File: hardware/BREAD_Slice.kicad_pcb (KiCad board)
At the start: 2 copper layers, 72.6 x 100 mm, 16 parts, among them J1 Conn_01x10_Female, J2 I2C_01x04

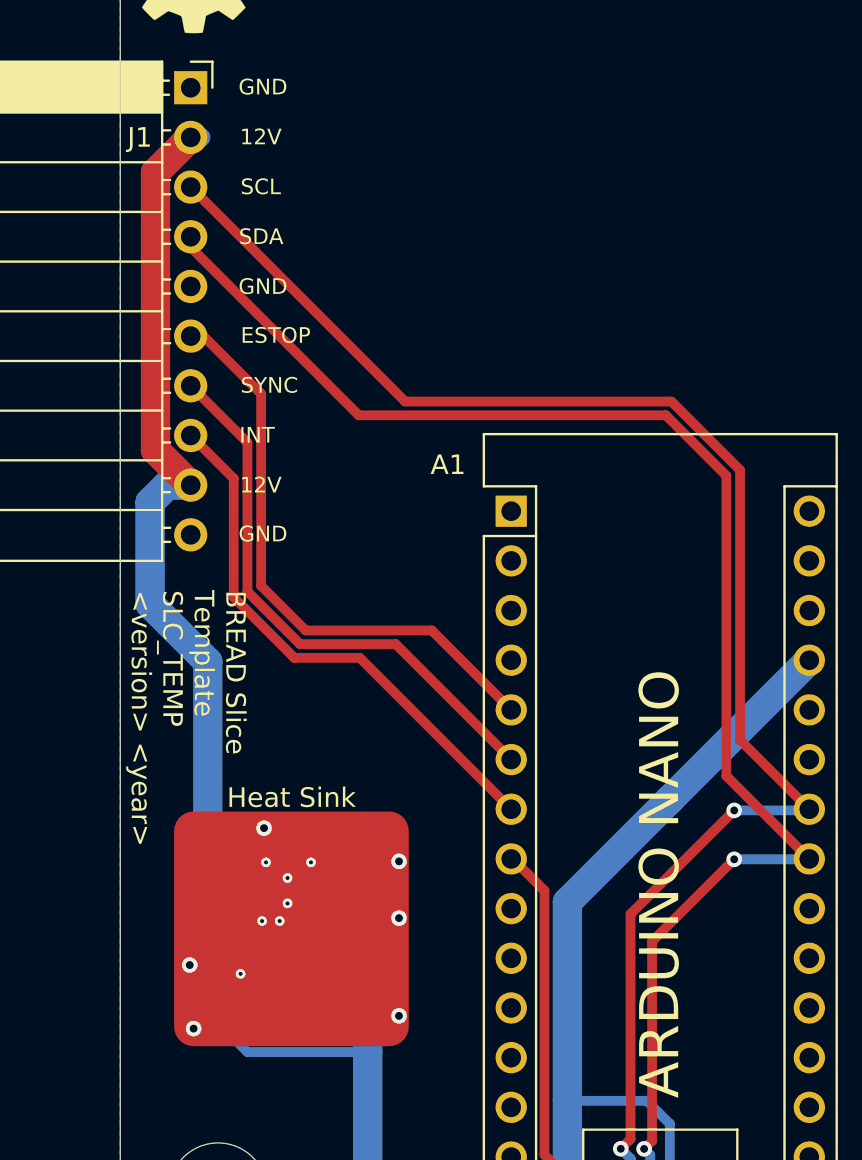
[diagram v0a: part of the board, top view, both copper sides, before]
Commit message: fixed 5-12V converter reinitializing placement when pcb is updated
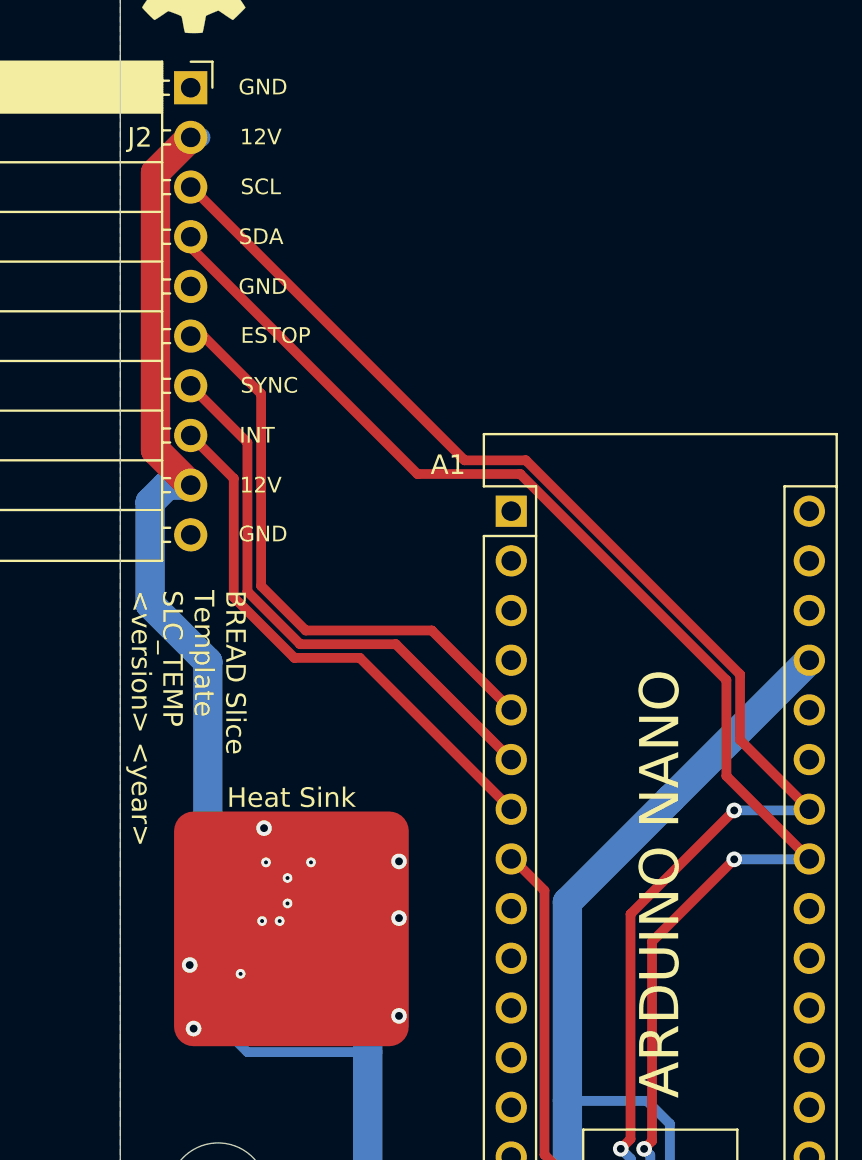
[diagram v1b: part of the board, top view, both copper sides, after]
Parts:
- HS1: footprint SparkFun-Fuse:Thermal Pad -> KML-Custom:Thermal Pad
- renumbered J2 to J1, J1 to J2
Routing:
- net /I2C_CLK: track 78.5 -> 72.3 mm
- net /I2C_DAT: track 76.6 -> 70.5 mm

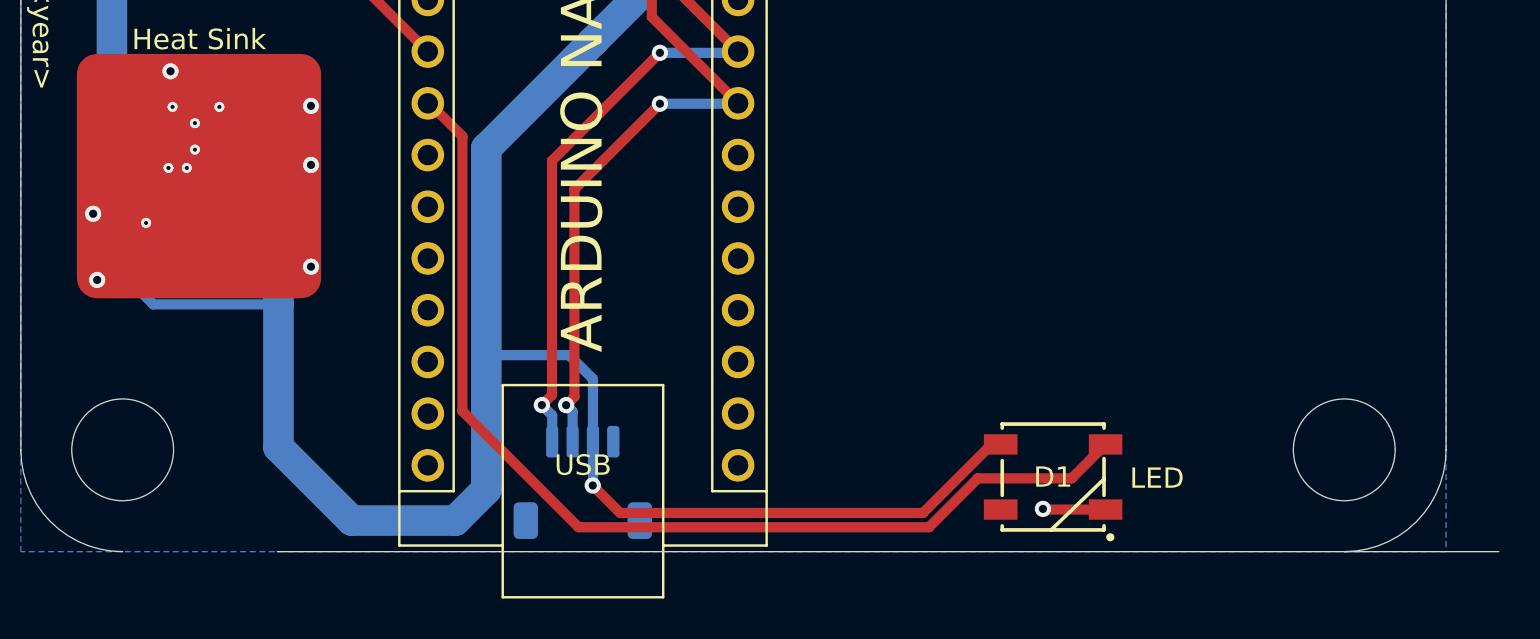
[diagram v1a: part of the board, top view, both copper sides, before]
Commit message: clear all DRC errors related to via placement and rules and also misplaced edge cuts
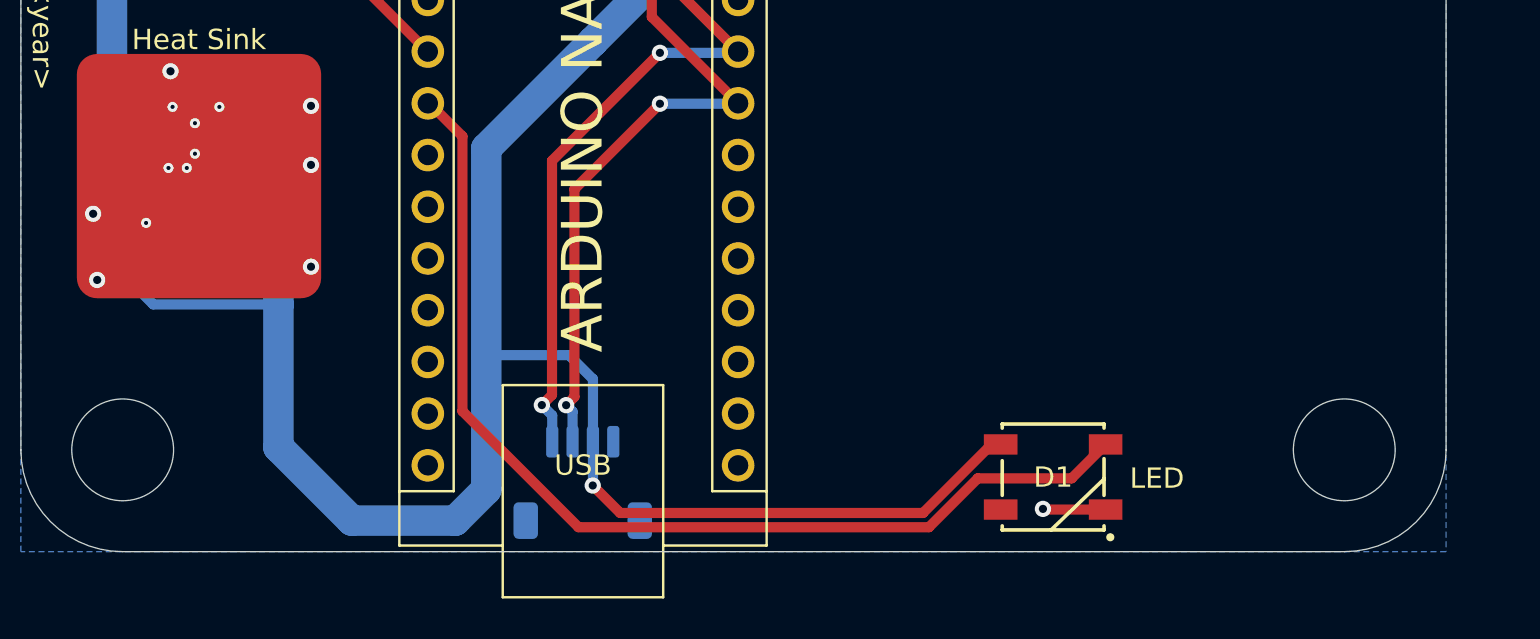
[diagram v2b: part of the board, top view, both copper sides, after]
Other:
- board size 72.6 x 100 mm -> 70 x 100 mm
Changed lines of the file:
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@@
 		(tags "TSOT TO_SOT_SMD")
 		(property "Reference" "U1"
-			(at 0 2.4 360)
+			(at 0 2.4 0)
 			(layer "B.SilkS")
 			(effects
@@
 		)
 		(fp_text user "${REFERENCE}"
-			(at 0 0 360)
+			(at 0 0 0)
 			(layer "B.Fab")
 			(effects
@@
 		(tags "capacitor")
 		(property "Reference" "C3"
-			(at 0 1.85 360)
+			(at 0 1.85 0)
 			(layer "B.SilkS")
 			(effects
@@
 		)
 		(property "Value" "22uF"
-			(at 0 -1.85 360)
+			(at 0 -1.85 0)
 			(layer "B.Fab")
 			(effects
@@
 		)
 		(fp_text user "${REFERENCE}"
-			(at 0 0 360)
+			(at 0 0 0)
 			(layer "B.Fab")
 			(effects
@@
 		(tags "capacitor")
 		(property "Reference" "C4"
-			(at 0 1.85 360)
+			(at 0 1.85 0)
 			(layer "B.SilkS")
 			(effects
@@
 		)
 		(property "Value" "22uF"
-			(at 0 -1.85 360)
+			(at 0 -1.85 0)
 			(layer "B.Fab")
 			(effects
@@
 		)
 		(fp_text user "${REFERENCE}"
-			(at 0 0 360)
+			(at 0 0 0)
 			(layer "B.Fab")
 			(effects
@@
 		)
 		(property "Value" "4.7uH"
-			(at 0 -2.28 360)
+			(at 0 -2.28 0)
 			(layer "B.Fab")
 			(effects
@@
 		)
 		(fp_text user "${REFERENCE}"
-			(at 0 0 360)
+			(at 0 0 0)
 			(layer "B.Fab")
 			(effects
@@
 	(gr_line
 		(start 160.188 139.8)
-		(end 195.188 139.8)
+		(end 187.6 139.8)
 		(stroke
 			(width 0.05)
@@
 	)
 	(gr_line
-		(start 135.188 139.8)
+		(start 127.6 139.8)
 		(end 160.188 139.8)
 		(stroke
@@
 		)
 	)
-	(dimension
-		(type aligned)
-		(layer "B.Cu")
-		(pts
-			(xy 127.6 44.8) (xy 187.6 44.8)
-		)
-		(height -5.6)
-		(gr_text "60.0000 mm"
-			(at 157.6 37.4 0)
-			(layer "B.Cu")
-			(effects
-				(font
-					(size 1.5 1.5)
-					(thickness 0.3)
-				)
-			)
-		)
-		(format
-			(prefix "")
-			(suffix "")
-			(units 3)
-			(units_format 1)
-			(precision 4)
-		)
-		(style
-			(thickness 0.2)
-			(arrow_length 1.27)
-			(text_position_mode 0)
-			(extension_height 0.58642)
-			(extension_offset 0.5) keep_text_aligned)
-	)
-	(dimension
-		(type aligned)
-		(layer "B.Cu")
-		(pts
-			(xy 179.6 21.6) (xy 249 21.6)
-		)
-		(height 3.2)
-		(gr_text "69.4000 mm"
-			(at 214.3 23 0)
-			(layer "B.Cu")
-			(effects
-				(font
-					(size 1.5 1.5)
-					(thickness 0.3)
-				)
-			)
-		)
-		(format
-			(prefix "")
-			(suffix "")
-			(units 3)
-			(units_format 1)
-			(precision 4)
-		)
-		(style
-			(thickness 0.2)
-			(arrow_length 1.27)
-			(text_position_mode 0)
-			(extension_height 0.58642)
-			(extension_offset 0.5) keep_text_aligned)
-	)
 	(segment
 		(start 172.8 137.7)
@@
 	)
 	(via
-		(at 131.15 120.055)
+		(at 131.15 120.255)
 		(size 0.5)
 		(drill 0.2)
@@
 	)
 	(segment
-		(start 131.15 119.455)
-		(end 131.15 118.755)
-		(width 0.5)
-		(layer "B.Cu")
-		(net 3)
-	)
-	(segment
 		(start 131 121.805)
 		(end 131.15 121.655)
@@
 	)
 	(segment
-		(start 131.15 119.455)
-		(end 131.15 120.055)
-		(width 0.5)
-		(layer "B.Cu")
-		(net 3)
-	)
-	(segment
 		(start 129.85 120.955)
 		(end 128.95 120.955)
@@
 	(segment
 		(start 131.15 119.455)
-		(end 132.375 119.455)
-		(width 1)
-		(layer "B.Cu")
-		(net 3)
-	)
-	(segment
-		(start 130.025 119.455)
-		(end 131.15 119.455)
-		(width 1)
-		(layer "B.Cu")
-		(net 3)
-	)
-	(segment
-		(start 131.15 120.055)
 		(end 131.15 120.255)
 		(width 0.5)
 		(layer "B.Cu")
 		(net 3)
+	)
+	(segment
+		(start 131.15 119.455)
+		(end 131.15 118.755)
+		(width 0.5)
+		(layer "B.Cu")
+		(net 3)
+	)
+	(segment
+		(start 130.025 119.455)
+		(end 132.375 119.455)
+		(width 1.5)
+		(layer "B.Cu")
+		(net 3)

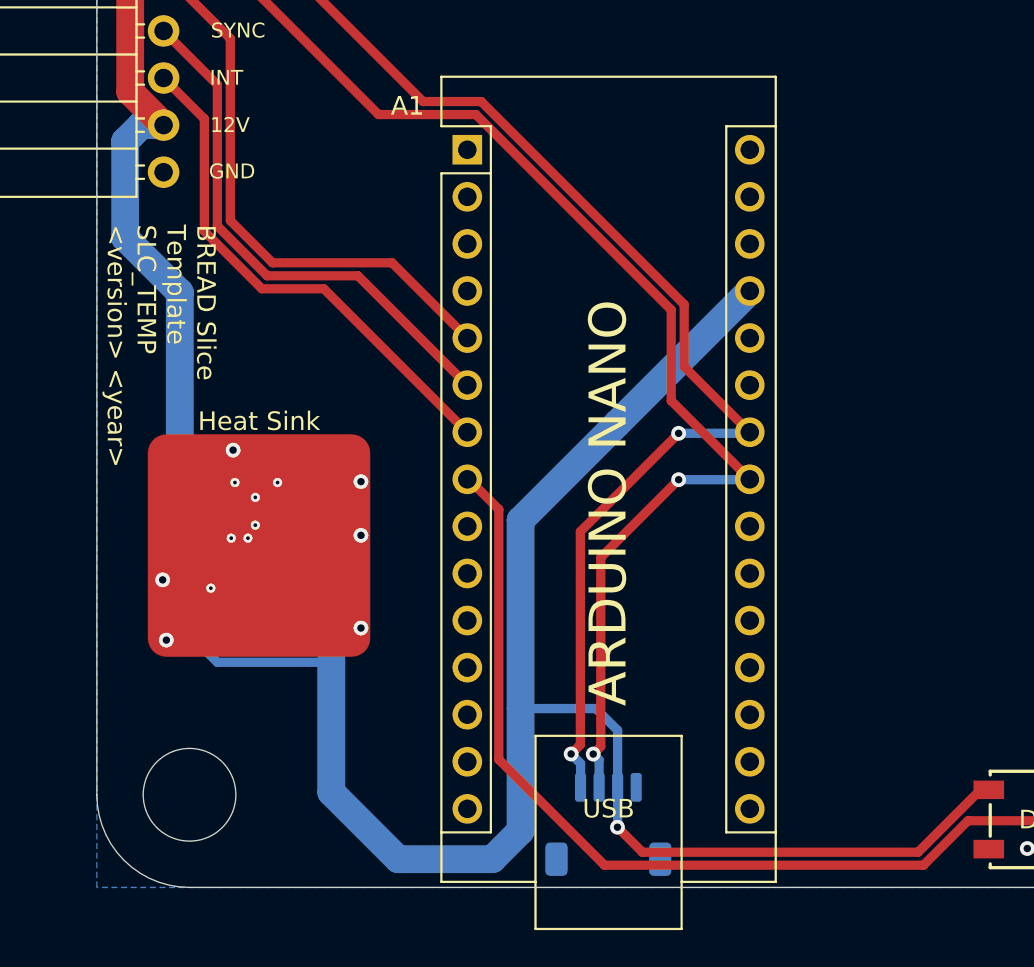
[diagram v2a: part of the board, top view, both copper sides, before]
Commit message: changed i2c connection to jst to simplify
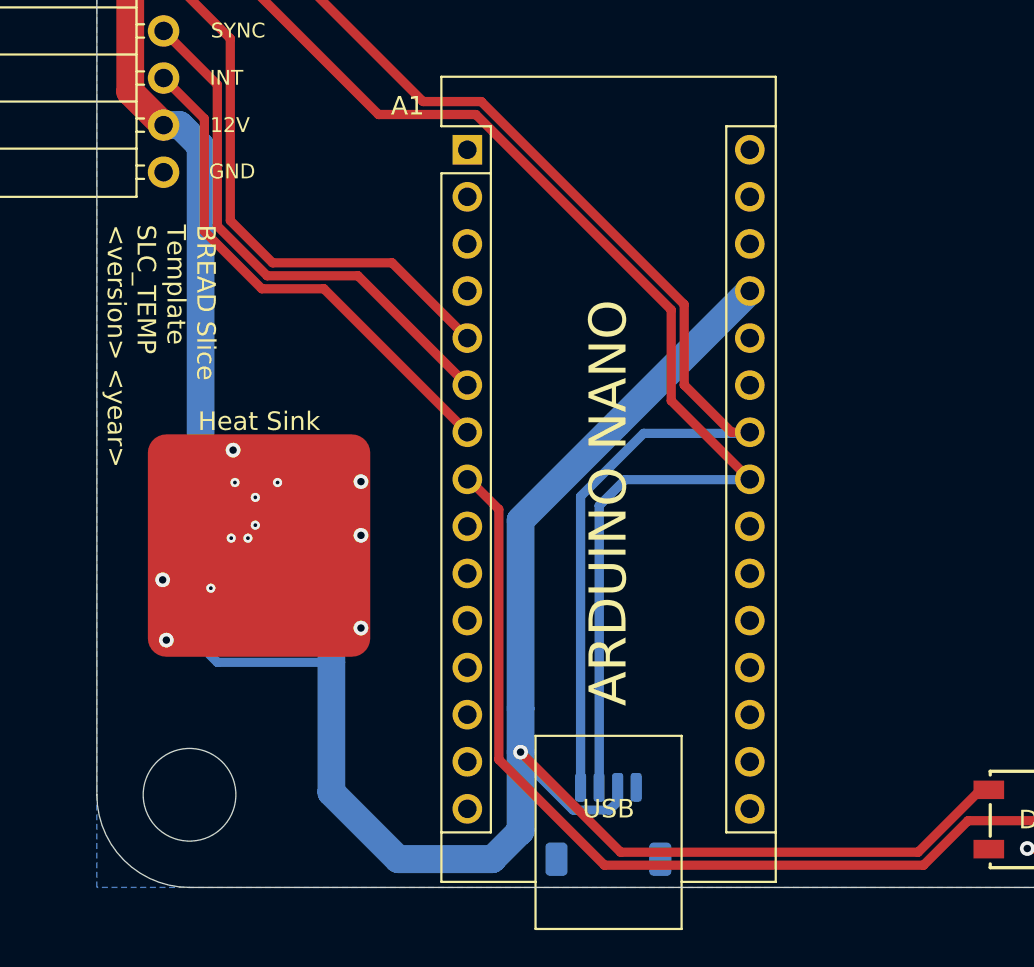
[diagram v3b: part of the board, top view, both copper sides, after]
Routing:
- net +5V: track 108.9 -> 112.5 mm
- net /I2C_DAT: track 70.5 -> 71.9 mm, vias 2 -> 0
- net /I2C_CLK: track 72.3 -> 73.6 mm, vias 2 -> 0
- net +12V: track 46.8 -> 45.9 mm
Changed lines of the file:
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@@
-	)
-	(segment
-		(start 152.0375 137.9)
-		(end 150.688 136.5505)
-		(width 0.5)
-		(layer "F.Cu")
-		(net 5)
 	)
 	(segment
@@
 	(segment
 		(start 166.91005 137.9)
-		(end 152.0375 137.9)
+		(end 150.86 137.9)
 		(width 0.5)
 		(layer "F.Cu")
@@
 	)
 	(segment
+		(start 150.86 137.9)
+		(end 145.46 132.5)
+		(width 0.5)
+		(layer "F.Cu")
+		(net 5)
+	)
+	(segment
 		(start 157.808 107.62)
 		(end 157.828 107.62)
@@
 	)
 	(via
-		(at 150.688 136.5505)
+		(at 145.46 132.5)
 		(size 0.8)
 		(drill 0.4)
@@
 	)
 	(segment
+		(start 145.46 132.789684)
+		(end 148.295316 135.625)
+		(width 0.5)
+		(layer "B.Cu")
+		(net 5)
+	)
+	(segment
 		(start 157.828 107.62)
 		(end 150.698 114.75)
@@
 	)
 	(segment
+		(start 150.247999 135.625)
+		(end 150.698 135.174999)
+		(width 0.5)
+		(layer "B.Cu")
+		(net 5)
+	)
+	(segment
 		(start 143.936 138.276)
 		(end 145.46 136.752)
@@
 	)
 	(segment
+		(start 145.46 132.5)
+		(end 145.46 132.789684)
+		(width 0.5)
+		(layer "B.Cu")
+		(net 5)
+	)
+	(segment
 		(start 135.25 127.655)
 		(end 129.103122 127.655)
@@
 	)
 	(segment
-		(start 149.524 130.148)
-		(end 145.46 130.148)
-		(width 0.5)
-		(layer "B.Cu")
-		(net 5)
-	)
-	(segment
 		(start 127.6125 126.164378)
 		(end 127.6125 123.705)
@@
 	)
 	(segment
-		(start 145.46 136.752)
+		(start 145.46 132.5)
 		(end 145.46 130.148)
 		(width 1.5)
-		(layer "B.Cu")
-		(net 5)
-	)
-	(segment
-		(start 150.698 134.4)
-		(end 150.698 131.322)
-		(width 0.5)
 		(layer "B.Cu")
 		(net 5)
@@
 	)
 	(segment
-		(start 150.698 136.5405)
-		(end 150.698 134.4)
-		(width 0.5)
-		(layer "B.Cu")
-		(net 5)
-	)
-	(segment
 		(start 135.3 116.48)
 		(end 135.3 119.43)
@@
 	)
 	(segment
+		(start 150.698 135.174999)
+		(end 150.698 134.4)
+		(width 0.5)
+		(layer "B.Cu")
+		(net 5)
+	)
+	(segment
 		(start 145.46 119.988)
 		(end 150.698 114.75)
@@
 	)
 	(segment
-		(start 150.688 136.5505)
-		(end 150.698 136.5405)
+		(start 148.295316 135.625)
+		(end 150.247999 135.625)
 		(width 0.5)
 		(layer "B.Cu")
@@
 	)
 	(segment
+		(start 145.46 136.752)
+		(end 145.46 132.5)
+		(width 1.5)
+		(layer "B.Cu")
+		(net 5)
+	)
+	(segment
 		(start 158.008 107.8)
 		(end 157.828 107.62)
@@
 	)
 	(segment
-		(start 150.698 131.322)
-		(end 149.524 130.148)
-		(width 0.5)
-		(layer "B.Cu")
-		(net 5)
-	)
-	(segment
 		(start 135.25 134.67)
 		(end 138.856 138.276)
@@
 	)
 	(segment
+		(start 156.84 115.24)
+		(end 154.288 112.688)
+		(width 0.5)
+		(layer "F.Cu")
+		(net 7)
+	)
+	(segment
 		(start 154.288 108.34805)
 		(end 143.33995 97.4)
@@
 	)
 	(segment
-		(start 154.288 111.7)
+		(start 157.828 115.24)
+		(end 156.84 115.24)
+		(width 0.5)
+		(layer "F.Cu")
+		(net 7)
+	)
+	(segment
+		(start 154.288 112.688)
 		(end 154.288 108.34805)
+		(width 0.5)
+		(layer "F.Cu")
+		(net 7)
+	)
+	(segment
+		(start 140.2 97.4)
+		(end 126.23 83.43)
 		(width 0.5)
 		(layer "F.Cu")
@@
 	)
 	(segment
-		(start 140.2 97.4)
-		(end 126.23 83.43)
-		(width 0.5)
-		(layer "F.Cu")
-		(net 7)
-	)
-	(segment
-		(start 148.188 132.6)
-		(end 148.688 132.1)
-		(width 0.5)
-		(layer "F.Cu")
+		(start 157.768 115.3)
+		(end 152.1 115.3)
+		(width 0.5)
+		(layer "B.Cu")
+		(net 7)
+	)
+	(segment
+		(start 148.698 118.702)
+		(end 148.698 134.4)
+		(width 0.5)
+		(layer "B.Cu")
+		(net 7)
+	)
+	(segment
+		(start 152.1 115.3)
+		(end 148.698 118.702)
+		(width 0.5)
+		(layer "B.Cu")
 		(net 7)
 	)
 	(segment
 		(start 157.828 115.24)
-		(end 154.288 111.7)
-		(width 0.5)
-		(layer "F.Cu")
-		(net 7)
-	)
-	(segment
-		(start 148.688 132.1)
-		(end 148.688 120.6)
-		(width 0.5)
-		(layer "F.Cu")
-		(net 7)
-	)
-	(segment
-		(start 148.688 120.6)
-		(end 153.988 115.3)
-		(width 0.5)
-		(layer "F.Cu")
-		(net 7)
-	)
-	(via
-		(at 148.188 132.6)
-		(size 0.8)
-		(drill 0.4)
-		(layers "F.Cu" "B.Cu")
-		(net 7)
-	)
-	(via
-		(at 153.988 115.3)
-		(size 0.8)
-		(drill 0.4)
-		(layers "F.Cu" "B.Cu")
-		(net 7)
-	)
-	(segment
-		(start 157.768 115.3)
-		(end 157.828 115.24)
-		(width 0.5)
-		(layer "B.Cu")
-		(net 7)
-	)
-	(segment
-		(start 148.188 132.6)
-		(end 148.698 133.11)
-		(width 0.5)
-		(layer "B.Cu")
-		(net 7)
-	)
-	(segment
-		(start 148.698 133.11)
-		(end 148.698 134.4)
-		(width 0.5)
-		(layer "B.Cu")
-		(net 7)
-	)
-	(segment
-		(start 153.988 115.3)
 		(end 157.768 115.3)
 		(width 0.5)
@@
 	)
 	(segment
-		(start 149.381039 132.604917)
-		(end 149.788 132.197956)
-		(width 0.5)
-		(layer "F.Cu")
-		(net 9)
-	)
-	(segment
 		(start 126.2 85.97)
 		(end 126.2 86.504)
@@
 	)
 	(segment
-		(start 149.788 132.197956)
-		(end 149.788 122)
-		(width 0.5)
-		(layer "F.Cu")
-		(net 9)
-	)
-	(segment
 		(start 126.2 86.504)
 		(end 137.796 98.1)
@@
 	)
 	(segment
-		(start 149.788 122)
-		(end 153.988 117.8)
-		(width 0.5)
-		(layer "F.Cu")
-		(net 9)
-	)
-	(via
-		(at 153.988 117.8)
-		(size 0.8)
-		(drill 0.4)
-		(layers "F.Cu" "B.Cu")
-		(net 9)
-	)
-	(via
-		(at 149.381039 132.604917)
-		(size 0.8)
-		(drill 0.4)
-		(layers "F.Cu" "B.Cu")
+		(start 149.698 134.4)
+		(end 149.698 119.202)
+		(width 0.5)
+		(layer "B.Cu")
+		(net 9)
+	)
+	(segment
+		(start 149.698 119.202)
+		(end 151.1 117.8)
+		(width 0.5)
+		(layer "B.Cu")
 		(net 9)
 	)
@@
 	)
 	(segment
-		(start 149.381039 132.604917)
-		(end 149.698 132.921878)
-		(width 0.5)
-		(layer "B.Cu")
-		(net 9)
-	)
-	(segment
-		(start 153.988 117.8)
+		(start 151.1 117.8)
 		(end 157.808 117.8)
-		(width 0.5)
-		(layer "B.Cu")
-		(net 9)
-	)
-	(segment
-		(start 149.698 132.921878)
-		(end 149.698 134.4)
 		(width 0.5)
 		(layer "B.Cu")
@@
 	)
 	(segment
-		(start 124.124 99.543919)
-		(end 124.124 104.748)
-		(width 1.5)
-		(layer "B.Cu")
-		(net 20)
-	)
-	(segment
-		(start 124.997919 98.67)
-		(end 124.124 99.543919)
-		(width 1.5)
-		(layer "B.Cu")
-		(net 20)
-	)
-	(segment
 		(start 126.71 80.89)
 		(end 126.2 80.89)
@@
 	)
 	(segment
-		(start 126.2 98.67)
-		(end 124.997919 98.67)
-		(width 1.5)
-		(layer "B.Cu")
-		(net 20)
-	)
-	(segment
 		(start 127.075 121.2675)
 		(end 127.6125 121.805)
@@
 	)
 	(segment
-		(start 124.124 104.748)
-		(end 127.075 107.699)
-		(width 1.5)
-		(layer "B.Cu")
-		(net 20)
-	)
-	(segment
-		(start 127.075 107.699)
+		(start 127.07 98.67)
+		(end 128.2 99.8)
+		(width 1.5)
+		(layer "B.Cu")
+		(net 20)
+	)
+	(segment
+		(start 128.2 118.33)
 		(end 127.075 119.455)
 		(width 1.5)
 		(layer "B.Cu")
+		(net 20)
+	)
+	(segment
+		(start 128.2 99.8)
+		(end 128.2 118.33)
+		(width 1.5)
+		(layer "B.Cu")
+		(net 20)
+	)
+	(segment
+		(start 126.2 98.67)
+		(end 127.07 98.67)
+		(width 1.5)
+		(layer "B.Cu")
